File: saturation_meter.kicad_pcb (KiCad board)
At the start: 2 copper layers, 48 parts, among them J1 Vin, J2 DUT, J3 Inputs, J4 Outputs, J5 UC, Q1 BUK556, Q2 BUK556, Q3 BC328, U1 LF33_TO220, U2 IR2112

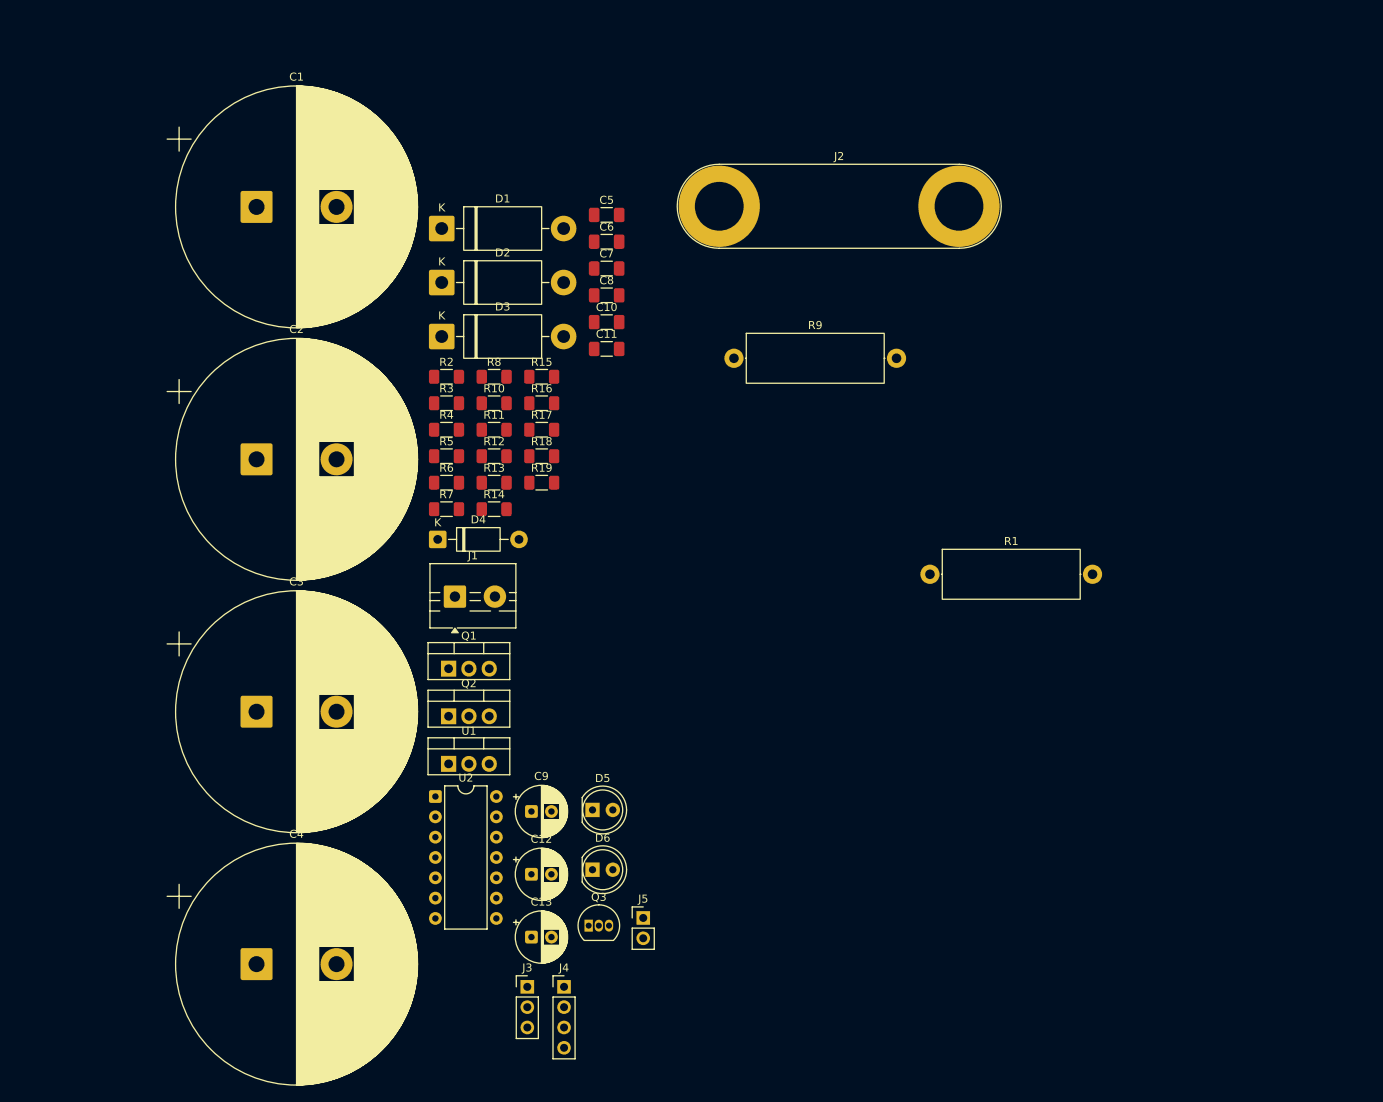
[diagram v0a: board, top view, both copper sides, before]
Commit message: First version of PCB, ready to isolation milling
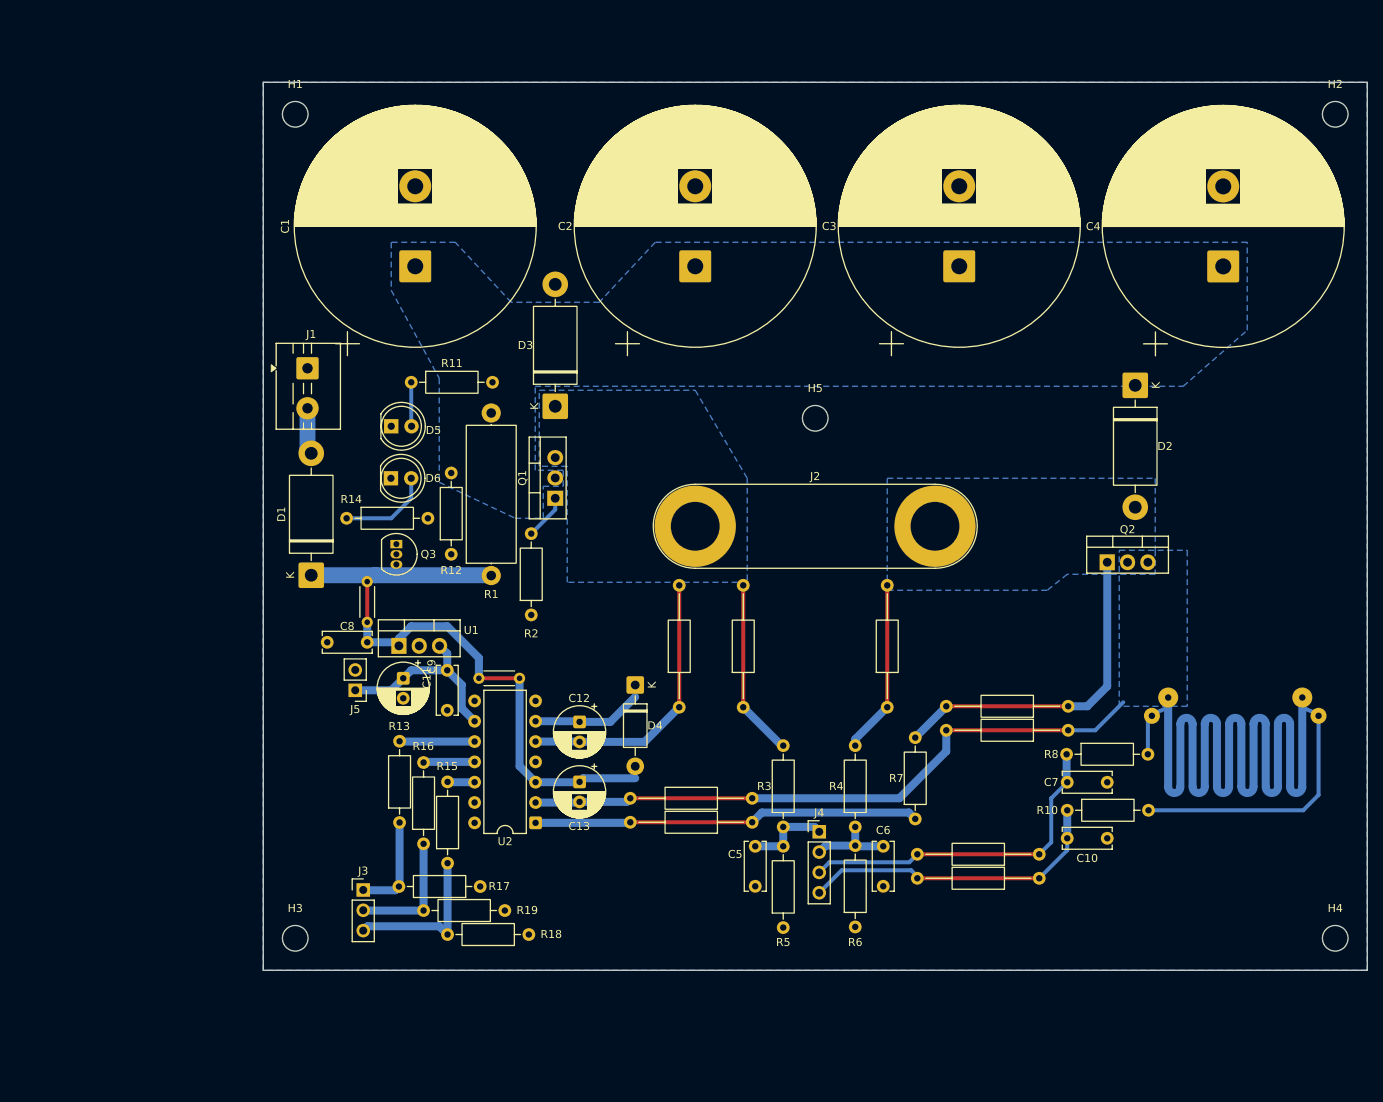
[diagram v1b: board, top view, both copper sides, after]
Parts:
- added H1: MountingHole, MountingHole:MountingHole_3.2mm_M3_DIN965, F.Cu at (113.5, 49.5)
- added H2: MountingHole, MountingHole:MountingHole_3.2mm_M3_DIN965, F.Cu at (243.5, 49.5)
- added H3: MountingHole, MountingHole:MountingHole_3.2mm_M3_DIN965, F.Cu at (113.5, 152.5)
- added H4: MountingHole, MountingHole:MountingHole_3.2mm_M3_DIN965, F.Cu at (243.5, 152.5)
- added H5: MountingHole, MountingHole:MountingHole_3.2mm_M3_DIN965, F.Cu at (178.5, 87.5)
- added REF**: R_Axial_DIN0207_L6.3mm_D2.5mm_P15.24mm_Horizontal, Resistor_THT:R_Axial_DIN0207_L6.3mm_D2.5mm_P15.24mm_Horizontal, F.Cu at (210.1, 123.5)
- added REF**: R_Axial_DIN0207_L6.3mm_D2.5mm_P15.24mm_Horizontal, Resistor_THT:R_Axial_DIN0207_L6.3mm_D2.5mm_P15.24mm_Horizontal, F.Cu at (170.6, 135.0)
- added REF**: R_Axial_DIN0207_L6.3mm_D2.5mm_P15.24mm_Horizontal, Resistor_THT:R_Axial_DIN0207_L6.3mm_D2.5mm_P15.24mm_Horizontal, F.Cu at (206.5, 145.0)
- added REF**: R_Axial_DIN0207_L6.3mm_D2.5mm_P15.24mm_Horizontal, Resistor_THT:R_Axial_DIN0207_L6.3mm_D2.5mm_P15.24mm_Horizontal, F.Cu at (210.1, 126.5)
- added REF**: R_Axial_DIN0207_L6.3mm_D2.5mm_P15.24mm_Horizontal, Resistor_THT:R_Axial_DIN0207_L6.3mm_D2.5mm_P15.24mm_Horizontal, F.Cu at (161.5, 123.6)
- added REF**: R_Axial_DIN0207_L6.3mm_D2.5mm_P15.24mm_Horizontal, Resistor_THT:R_Axial_DIN0207_L6.3mm_D2.5mm_P15.24mm_Horizontal, F.Cu at (187.5, 123.6)
- added REF**: R_Axial_DIN0204_L3.6mm_D1.6mm_P5.08mm_Horizontal, Resistor_THT:R_Axial_DIN0204_L3.6mm_D1.6mm_P5.08mm_Horizontal, F.Cu at (122.5, 113.0)
- added REF**: R_Axial_DIN0207_L6.3mm_D2.5mm_P15.24mm_Horizontal, Resistor_THT:R_Axial_DIN0207_L6.3mm_D2.5mm_P15.24mm_Horizontal, F.Cu at (206.5, 142.0)
- added REF**: R_Axial_DIN0204_L3.6mm_D1.6mm_P5.08mm_Horizontal, Resistor_THT:R_Axial_DIN0204_L3.6mm_D1.6mm_P5.08mm_Horizontal, F.Cu at (141.5, 120.0)
- added REF**: R_Axial_DIN0207_L6.3mm_D2.5mm_P15.24mm_Horizontal, Resistor_THT:R_Axial_DIN0207_L6.3mm_D2.5mm_P15.24mm_Horizontal, F.Cu at (169.5, 123.6)
- added REF**: R_Axial_DIN0207_L6.3mm_D2.5mm_P15.24mm_Horizontal, Resistor_THT:R_Axial_DIN0207_L6.3mm_D2.5mm_P15.24mm_Horizontal, F.Cu at (170.6, 138.0)
- C10, C11, C5, C6, C7, C8: footprint Capacitor_SMD:C_1206_3216Metric_Pad1.33x1.80mm_HandSolder -> Capacitor_THT:C_Disc_D6.0mm_W2.5mm_P5.00mm
- R10, R11, R12, R13, R14, R15, R16, R17, R18, R19, R2, R3, R4, R5, R6, R7, R8: footprint Resistor_SMD:R_1206_3216Metric_Pad1.30x1.75mm_HandSolder -> Resistor_THT:R_Axial_DIN0207_L6.3mm_D2.5mm_P10.16mm_Horizontal
- R9: value 10m -> 60m; footprint Resistor_THT:R_Axial_DIN0617_L17.0mm_D6.0mm_P20.32mm_Horizontal -> shunt:R_Shunt_kelvin_60mohm
- moved C4 149.0 mm to (229.5, 68.5), turned to 90 degrees
- moved C3 104.0 mm to (196.5, 68.5), turned to 90 degrees
- moved R10 87.9 mm to (210.0, 136.5)
- moved D2 87.6 mm to (218.5, 83.4), turned to -90 degrees
- moved C10 86.5 mm to (210.0, 140.0)
- moved C7 86.2 mm to (210.0, 133.0)
- moved R8 85.7 mm to (209.9, 129.5)
- moved Q2 84.6 mm to (215.0, 105.5)
- moved C6 83.1 mm to (187.0, 141.0), turned to -90 degrees
- moved R9 83.1 mm to (232.0, 133.3), turned to 90 degrees
- moved C5 81.1 mm to (171.0, 141.0), turned to -90 degrees
- moved R6 75.5 mm to (183.5, 151.1), turned to 90 degrees
- moved R5 72.4 mm to (174.5, 151.2), turned to 90 degrees
- moved R4 71.2 mm to (183.5, 138.6), turned to 90 degrees
- moved R7 70.2 mm to (191.0, 137.6), turned to 90 degrees
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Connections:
- net Net-(D4-K) renamed /vb
- net Net-(U2-HIN) renamed /hin
- net Net-(U2-LIN) renamed /lin
- net Net-(U2-SD) renamed /sd
- C13 pad 1: /vbus -> /vin_prot
- C8 pad 1: /vbus -> /vin_prot
- D1 pad 1: /charge_det -> /vin_prot
- D4 pad 2: /vbus -> /vin_prot
- J3 pad 2: /lin_uc -> /sd_uc
- J3 pad 3: /sd_uc -> /lin_uc
- J4 pad 1: /i_sense_high -> /dut_high
- J4 pad 2: /i_sense_low -> /dut_low
- J4 pad 3: /dut_high -> /i_sense_high
- J4 pad 4: /dut_low -> /i_sense_low
- Q2 pad 3: /low_nmos_g -> /low_nmos_s
- Q3 pad 3: /charge_det -> /vin_prot
- R1 pad 1: /charge_det -> /vin_prot
- R10 pad 2: GND -> Net-(R10-Pad2)
- R7 pad 1: /driver_ho -> /driver_lo
- R8 pad 2: /low_nmos_g -> Net-(R8-Pad2)
- R9 pad 1: /low_nmos_g -> /low_nmos_s
- R9 pad 2: GND -> Net-(R8-Pad2)
- U1 pad 1: /vbus -> /vin_prot
- U2 pad 3: /vbus -> /vin_prot
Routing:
- net /vin_prot: track 0.00 -> 81.6 mm
- net /low_nmos_s: track 0.00 -> 80.2 mm
- net /high_nmos_s: track 0.00 -> 60.4 mm
- net /driver_lo: track 0.00 -> 48.3 mm
- net /i_sense_high: track 0.00 -> 42.3 mm
- net /low_nmos_g: track 0.00 -> 42.2 mm
- net /i_sense_low: track 0.00 -> 39.2 mm
- net Net-(R10-Pad2): track 0.00 -> 32.2 mm
- net +3.3V: track 0.00 -> 23.8 mm
- net /low_nmos_d: track 0.00 -> 21.7 mm
- net /lin_uc: track 0.00 -> 20.1 mm
- net /sd_uc: track 0.00 -> 15.9 mm
- net /vb: track 0.00 -> 13.8 mm
- net /hin_uc: track 0.00 -> 12.7 mm
- net Net-(D6-A): track 0.00 -> 11.6 mm
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- added copper zone on B.Cu, net /high_nmos_s
- added copper zone on B.Cu, net /low_nmos_d
- added copper zone on B.Cu, net /low_nmos_s
- added copper zone on B.Cu, net /vbus
- added copper zone on B.Cu, net GND
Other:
- board outline added: 138 x 111 mm

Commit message: Added version number
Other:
- board text added: "1.0.0"
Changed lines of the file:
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@@
 		(layer "Edge.Cuts")
+	)
+	(gr_text "1.0.0"
+		(at 239 155 0)
+		(layer "B.Cu")
+		(effects
+			(font
+				(size 4 4)
+				(thickness 1)
+				(bold yes)
+			)
+			(justify left bottom mirror)
+		)
 	)
 	(dimension

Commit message: Added pictures and updated design sheet
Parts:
- moved R13 31.8 mm to (95.7, 130.5)
- moved R17 31.8 mm to (105.7, 138.5)
- moved C1 31.8 mm to (97.6, 61.0)
- moved C10 31.8 mm to (179.1, 132.5)
- moved C11 31.8 mm to (101.6, 111.5)
- moved C12 31.8 mm to (118.2, 118.0)
- moved C2 31.8 mm to (132.6, 61.0)
- moved C3 31.8 mm to (165.6, 61.0)
- moved C5 31.8 mm to (140.1, 133.5)
- moved C6 31.8 mm to (156.1, 133.5)
- moved C7 31.8 mm to (179.1, 125.5)
- moved C8 31.8 mm to (91.6, 108.0)
- moved C9 31.8 mm to (96.1, 112.5)
- moved D1 31.8 mm to (84.6, 99.6)
- moved D2 31.8 mm to (187.6, 75.9)
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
